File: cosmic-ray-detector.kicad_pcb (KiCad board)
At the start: 2 copper layers, 98.6 x 96 mm, 59 parts, among them J1 15-91-0060, J2 15-91-0060, J3 SJ-43515RS-SMT, U1 LT3461, U2 LT1807, U3 Arduino_Nano_v3.x

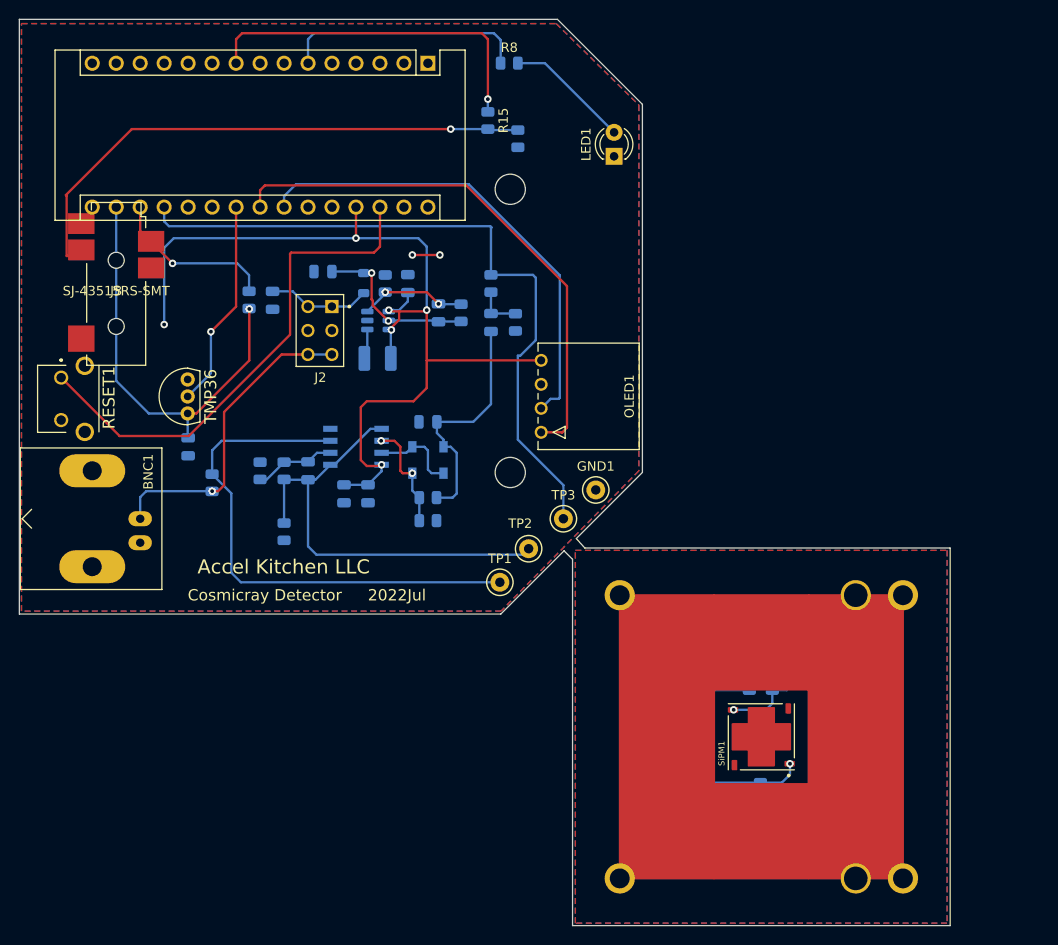
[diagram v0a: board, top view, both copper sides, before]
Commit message: Add KiCad PCB project, CAD models, gerbers, libraries, and outputs
Track the full hardware project: KiCad schematic/PCB sources (v2 and
split variants), component libraries and 3D shapes, fabrication outputs
(gerbers, drill, position/BOM CSVs, STEP/STL/WRL), CAD enclosure models,
schematic exports (SVG/PDF), SPICE models, and reference photos.

Co-Authored-By: Claude Opus 4.8 <noreply@anthropic.com>
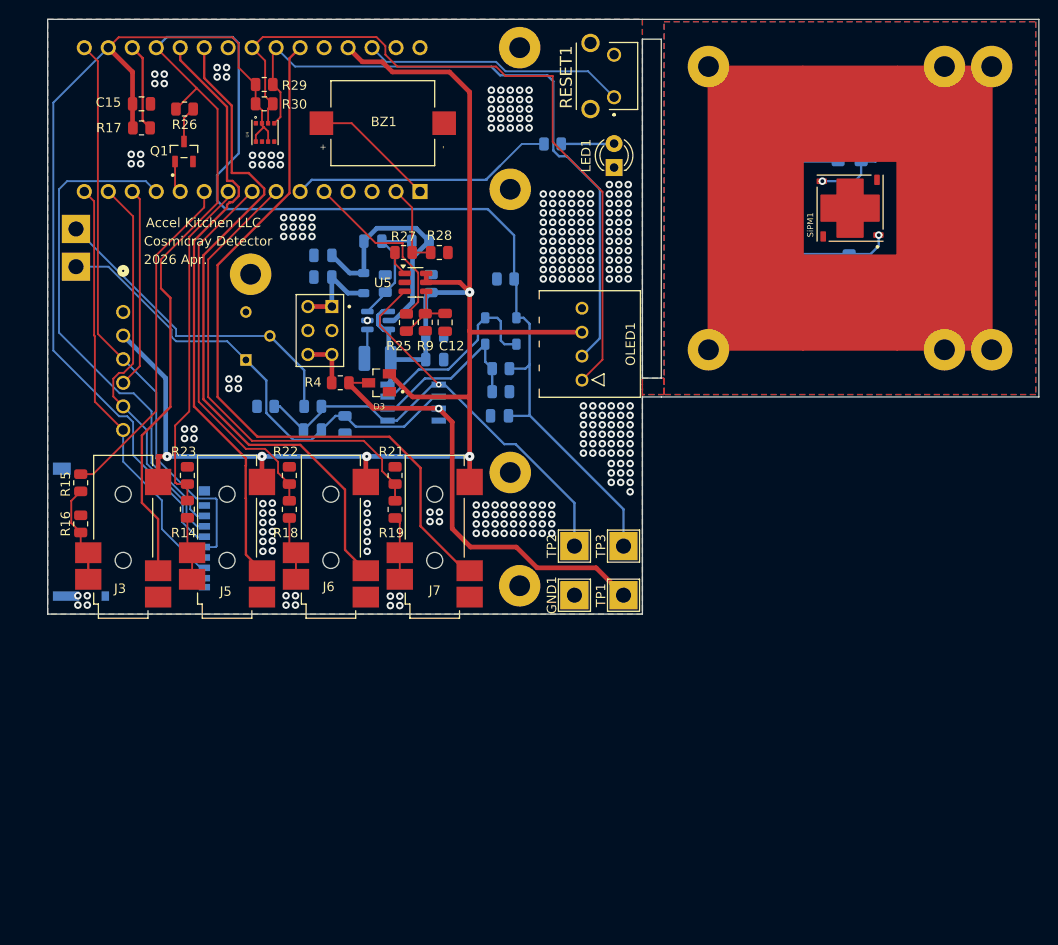
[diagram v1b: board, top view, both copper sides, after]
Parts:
- removed BNC1: Conn_Coaxial, Connector_Coaxial:BNC_Amphenol_B6252HB-NPP3G-50_Horizontal
- removed C14: short, Capacitor_SMD:C_0805_2012Metric
- removed the REF** at (131.6, 127.0)
- removed the REF** at (131.6, 97.0)
- removed the REF** at (101.6, 97.0)
- removed the REF** at (90.0, 54.0)
- removed the REF** at (101.6, 127.0)
- removed the REF** at (126.6, 127.0)
- removed the REF** at (126.6, 97.0)
- removed the REF** at (90.0, 84.0)
- removed TMP36: TMP36GT9Z, SamacSys_Parts:TO-92
- added BZ1: CPT-1117-83-SMT-TR, SamacSys_Parts:XDCR_CPT-1117-83-SMT-TR, F.Cu at (76.5, 47.0)
- added C12: 1u, Capacitor_SMD:C_0805_2012Metric, F.Cu at (83.1, 68.1)
- added D3: BAT54S, SamacSys_Parts:SOT95P240X120-3N, F.Cu at (76.1, 74.5)
- added J4: S6B-XH-A-1, cosmic-ray-detector:CONN_S6B-XH-A-1_JST, B.Cu at (49.0, 67.0)
- added J5: SJ-43515RS-SMT, cosmic-ray-detector:SJ-43515RS-SMT-TR, F.Cu at (60.0, 90.1)
- added J6: SJ-43515RS-SMT, cosmic-ray-detector:SJ-43515RS-SMT-TR, F.Cu at (71.0, 90.1)
- added J7: SJ-43515RS-SMT, cosmic-ray-detector:SJ-43515RS-SMT-TR, F.Cu at (82.0, 90.1)
- added J8: DM3AT-SF-PEJM5, cosmic-ray-detector:HRS_DM3AT-SF-PEJM5, B.Cu at (49.6, 90.3)
- added Q1: 2N7002, SamacSys_Parts:SOT95P240X111-3N, F.Cu at (55.4, 50.0)
- added R10: 3362P-1-103LF, SamacSys_Parts:TRIM_3362P-1-103LF, B.Cu at (62.0, 69.5)
- added R14: 1k, Resistor_SMD:R_0805_2012Metric, F.Cu at (55.8, 87.9)
- added R18: 1k, Resistor_SMD:R_0805_2012Metric, F.Cu at (66.6, 87.9)
- added R19: 1k, Resistor_SMD:R_0805_2012Metric, F.Cu at (77.8, 87.9)
- added R21: 10k, Resistor_SMD:R_0805_2012Metric, F.Cu at (77.8, 84.3)
- added R22: 10k, Resistor_SMD:R_0805_2012Metric, F.Cu at (66.6, 84.3)
- added R23: 10k, Resistor_SMD:R_0805_2012Metric, F.Cu at (55.8, 84.3)
- added R25: 1K, Resistor_SMD:R_0805_2012Metric, F.Cu at (79.0, 68.1)
- added R26: 1K, Resistor_SMD:R_0805_2012Metric, F.Cu at (55.5, 45.5)
- added R27: 1K, Resistor_SMD:R_0805_2012Metric, F.Cu at (78.7, 60.7)
- added R28: 2K, Resistor_SMD:R_0805_2012Metric, F.Cu at (82.5, 60.7)
- added R29: 4.7K, Resistor_SMD:R_0805_2012Metric, F.Cu at (63.9, 42.9)
- added R30: 4.7K, Resistor_SMD:R_0805_2012Metric, F.Cu at (63.9, 45.0)
- added REF**: MountingHole_2.2mm_M2_Pad, MountingHole:MountingHole_2.2mm_M2_Pad, F.Cu at (91.0, 96.0)
- added REF**: MountingHole_2.2mm_M2_Pad, MountingHole:MountingHole_2.2mm_M2_Pad, F.Cu at (90.0, 84.0)
- added REF**: MountingHole_2.2mm_M2_Pad, MountingHole:MountingHole_2.2mm_M2_Pad, F.Cu at (90.0, 54.0)
- added REF**: MountingHole_2.2mm_M2_Pad, MountingHole:MountingHole_2.2mm_M2_Pad, F.Cu at (141.0, 71.0)
- added REF**: MountingHole_2.2mm_M2_Pad, MountingHole:MountingHole_2.2mm_M2_Pad, F.Cu at (111.0, 71.0)
- added REF**: MountingHole_2.2mm_M2_Pad, MountingHole:MountingHole_2.2mm_M2_Pad, F.Cu at (62.5, 63.0)
- added REF**: MountingHole_2.2mm_M2_Pad, MountingHole:MountingHole_2.2mm_M2_Pad, F.Cu at (111.0, 41.0)
- added REF**: MountingHole_2.2mm_M2_Pad, MountingHole:MountingHole_2.2mm_M2_Pad, F.Cu at (141.0, 41.0)
- added REF**: MountingHole_2.2mm_M2_Pad, MountingHole:MountingHole_2.2mm_M2_Pad, F.Cu at (91.0, 39.0)
- added REF**: MountingHole_2.2mm_M2_Pad, MountingHole:MountingHole_2.2mm_M2_Pad, F.Cu at (136.0, 41.0)
- added REF**: MountingHole_2.2mm_M2_Pad, MountingHole:MountingHole_2.2mm_M2_Pad, F.Cu at (136.0, 71.0)
- added TP4: TestPoint, TestPoint:TestPoint_THTPad_3.0x3.0mm_Drill1.5mm, B.Cu at (44.0, 58.2)
- added TP5: TestPoint, TestPoint:TestPoint_THTPad_3.0x3.0mm_Drill1.5mm, B.Cu at (44.0, 62.2)
- added U4: BME280, SamacSys_Parts:PSON65P250X250X100-8N, F.Cu at (64.0, 48.0)
- added U5: LT1806CS6-TRMPBF, Package_TO_SOT_SMD:TSOT-23-6, F.Cu at (80.0, 63.9)
- C15, R15, R16, R17, R4: moved to F.Cu
- GND1, TP1, TP2, TP3: footprint TestPoint:TestPoint_Keystone_5000-5004_Miniature -> TestPoint:TestPoint_THTPad_3.0x3.0mm_Drill1.5mm
- R5: value 10k -> 1k
- R9: value short -> 1K; moved to F.Cu
- U3: moved to B.Cu
- moved RESET1 66.5 mm to (100.2, 42.0), turned to 90 degrees
- moved R16 61.7 mm to (44.5, 89.4), turned to 90 degrees
- moved R15 57.7 mm to (44.5, 85.1)
- moved SiPM1 56.8 mm to (126.0, 56.0)
- moved C10 56.8 mm to (124.7, 46.3)
- moved C8 56.8 mm to (127.2, 46.3)
- moved C9 56.8 mm to (129.6, 46.3)
- moved J1 56.8 mm to (115.6, 56.5)
- moved R11 56.8 mm to (127.2, 50.1)
- moved R13 56.8 mm to (124.7, 50.1)
- moved C11 56.8 mm to (122.2, 46.3)
- moved R12 56.8 mm to (125.9, 61.8)
- moved C15 36.7 mm to (50.9, 45.0), turned to 0 degrees
- moved J3 25.3 mm to (49.0, 90.1), turned to 180 degrees
- moved R17 21.5 mm to (50.9, 47.5), turned to 180 degrees
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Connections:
- net Net-(C15-Pad1) renamed 3V
- net Net-(C18-Pad1) renamed HV
- net Net-(C7-Pad2) renamed Amplifier
- net Net-(OLED1-Pad1) renamed SDA
- net Net-(OLED1-Pad2) renamed SCL
- C3 pad 1: Net-(C3-Pad1) -> 5V
- C4 pad 1: Net-(C3-Pad1) -> 5V
- C5 pad 1: Net-(C3-Pad1) -> 5V
- C6 pad 1: Net-(C14-Pad2) -> ANA_OUT
- C7 pad 1: Net-(C7-Pad1) -> RES_VAL2
- D1 pad 1: Net-(C14-Pad2) -> ANA_OUT
- J3 pad 2: Net-(C3-Pad1) -> 5V
- J3 pad 4: unconnected-(J3-Pad4) -> ANA_OUT
- L1 pad 2: Net-(C3-Pad1) -> 5V
- OLED1 pad 3: GND -> 5V
- OLED1 pad 4: Net-(C3-Pad1) -> GND
- R15 pad 2: Net-(R15-Pad2) -> COIN_OUT
- R24 pad 1: Net-(C14-Pad1) -> ANA_OUT
- R3 pad 1: Net-(C7-Pad1) -> RES_VAL2
- R5 pad 2: Net-(C7-Pad1) -> RES_VAL
- R7 pad 2: Net-(C14-Pad2) -> ANA_OUT
- R9 pad 1: Net-(C14-Pad1) -> GND
- R9 pad 2: Net-(R9-Pad2) -> Net-(U5--IN)
- RESET1 pad 3: (no net) -> GND
- RESET1 pad 4: (no net) -> GND
- TP3 pad 1: Net-(R9-Pad2) -> ANA_OUT
- U1 pad 4: Net-(C3-Pad1) -> 5V
- U1 pad 6: Net-(C3-Pad1) -> 5V
- U2 pad 2: Net-(C7-Pad1) -> RES_VAL2
- U2 pad 8: Net-(C3-Pad1) -> 5V
- U3 pad 1: unconnected-(U3-Pad1) -> Net-(U3-D1/TX)
- U3 pad 10: unconnected-(U3-Pad10) -> COIN_OUT
- U3 pad 11: unconnected-(U3-Pad11) -> TriggerReset
- U3 pad 12: unconnected-(U3-Pad12) -> CS2
- U3 pad 13: unconnected-(U3-Pad13) -> CS1
- U3 pad 14: unconnected-(U3-Pad14) -> MOSI
- U3 pad 15: unconnected-(U3-Pad15) -> MISO
- U3 pad 16: unconnected-(U3-Pad16) -> SCLK
- U3 pad 19: Net-(R9-Pad2) -> ANA_OUT
- U3 pad 2: unconnected-(U3-Pad2) -> Trigger
- U3 pad 20: unconnected-(U3-Pad20) -> ANA_IN1
- U3 pad 21: unconnected-(U3-Pad21) -> ANA_IN2
- U3 pad 22: Net-(TMP36-Pad2) -> unconnected-(U3-A3-Pad22)
- U3 pad 25: unconnected-(U3-Pad25) -> ANA_IN3
- U3 pad 27: Net-(C3-Pad1) -> 5V
- U3 pad 5: unconnected-(U3-Pad5) -> PWM
- U3 pad 7: unconnected-(U3-Pad7) -> DIG_IN3
- U3 pad 8: unconnected-(U3-Pad8) -> DIG_IN2
- U3 pad 9: Net-(R15-Pad2) -> DIG_IN1
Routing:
- net ANA_OUT: track 0.00 -> 168.9 mm
- net 5V: track 0.00 -> 163.8 mm, vias 0 -> 5
- net Net-(C3-Pad1): track 101.2 -> 0.00 mm, vias 6 -> 0
- net ANA_IN3: track 0.00 -> 78.8 mm
- net Net-(R9-Pad2): track 75.3 -> 0.00 mm
- net ANA_IN2: track 0.00 -> 72.1 mm
- net ANA_IN1: track 0.00 -> 63.5 mm
- net SCLK: track 0.00 -> 60.7 mm
- net 3V: track 44.3 -> 99.5 mm, vias 1 -> 0
- net CS2: track 0.00 -> 53.4 mm
- net DIG_IN3: track 0.00 -> 50.9 mm
- net RES_VAL2: track 0.00 -> 50.9 mm
- net Net-(J3-Pad3): track 60.1 -> 9.35 mm, vias 1 -> 0
- net MISO: track 0.00 -> 45.0 mm
- net MOSI: track 0.00 -> 42.2 mm
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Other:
- board size 98.6 x 96 mm -> 105 x 63 mm
- board text added: "2026 Apr."
- board text added: "2026 Feb."
- board text removed: "2022Jul"
